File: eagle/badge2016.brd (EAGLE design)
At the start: 124.2 x 92.5 mm, 82 parts, among them IC1 FT230XS, IC3 24AA01SN, J1 USB-MICRO, Q2 BC857ALT1SMD, X1 PASSER-07, X2 PASSER-07, X3 PASSER-07

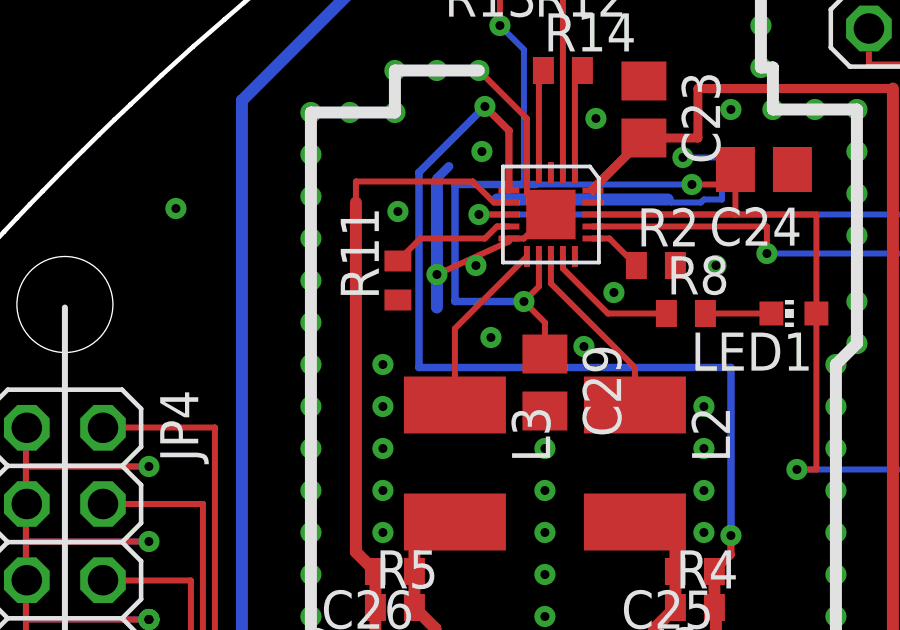
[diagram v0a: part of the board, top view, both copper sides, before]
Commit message: Update Layout changes by LTC3554 review
Review and changes LTC3554:
* Missing connecting Pin 9 (PWR_ON1) via R11 to Pin 18 (V_OUT) to activate SW1
* Change R2 from 1.87k to 750 (for max. load of 1A)
* PIN 15 (NTC) to GND, because NTC is not in use
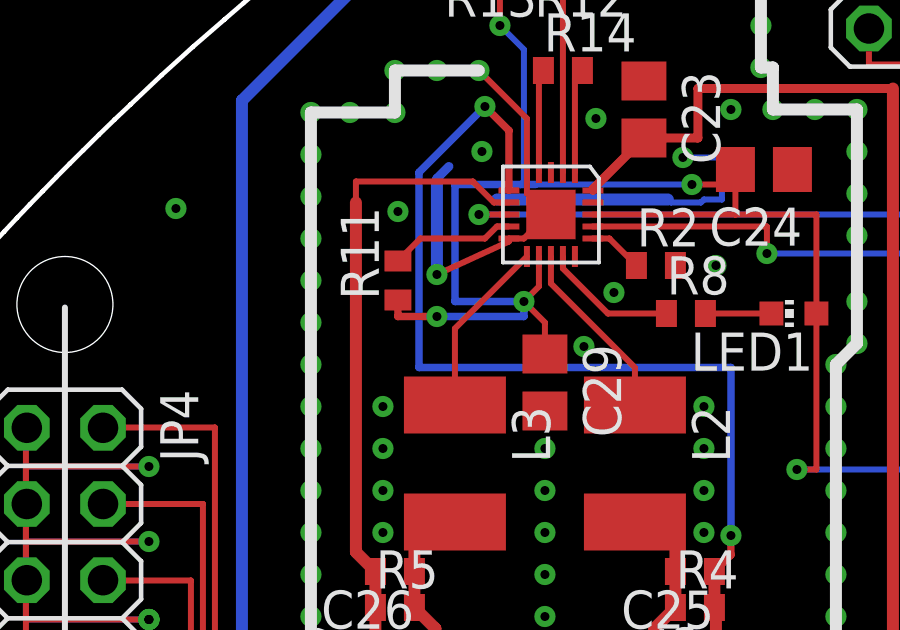
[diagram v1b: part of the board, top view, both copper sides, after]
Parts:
- R2: value 1.87k -> 750
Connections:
- removed net N$24: R11.1
- net GND: now also U$11.15
- net V_USB: now also R11.1
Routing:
- net V_USB: track 103.5 -> 108.7 mm, vias 7 -> 8
- net GND: track 298.7 -> 297.6 mm, vias 201 -> 198
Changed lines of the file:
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@@
 <element name="U$10" library="ERNW_parts" package="SMA_CON_THT" value="SMA_CONNECTORTHT" x="107.83" y="57.5"/>
 <element name="U$11" library="ERNW_parts" package="QFN-20-3X3" value="LTC3554" x="30.1" y="63" rot="R270"/>
-<element name="R2" library="rcl" package="R0402" value="1.87k" x="33.6" y="61.3"/>
+<element name="R2" library="rcl" package="R0402" value="750" x="33.6" y="61.3"/>
 <element name="C23" library="rcl" package="C0805" value="10µF" x="33.2" y="66.5" rot="R270"/>
 <element name="C24" library="rcl" package="C0805" value="10µF" x="37.2" y="64.5" rot="R180"/>
@@
 <wire x1="105.29" y1="60.04" x2="110.37" y2="60.04" width="0.4" layer="1"/>
 <wire x1="110.37" y1="60.04" x2="110.37" y2="54.96" width="0.4" layer="1"/>
-<contactref element="R2" pad="2"/>
 <contactref element="C23" pad="1"/>
 <contactref element="C24" pad="1"/>
@@
 <wire x1="54.4" y1="44.495" x2="54.4" y2="44.4" width="0.2" layer="1"/>
 <via x="68" y="47" extent="1-16" drill="0.3"/>
-<via x="27.6" y="61.3" extent="1-16" drill="0.3"/>
 <via x="26.3" y="61" extent="1-16" drill="0.3"/>
-<via x="28.1" y="58.9" extent="1-16" drill="0.3"/>
 <via x="32.2" y="60.4" extent="1-16" drill="0.3"/>
 <via x="27.8" y="65.1" extent="1-16" drill="0.3"/>
@@
 <via x="24.5" y="53.8" extent="1-16" drill="0.3"/>
 <via x="24.5" y="52.4" extent="1-16" drill="0.3"/>
-<via x="24.5" y="58" extent="1-16" drill="0.3"/>
 <via x="78.2" y="53.6" extent="1-16" drill="0.3"/>
 <via x="39.6" y="42.6" extent="1-16" drill="0.3"/>
@@
 <via x="51.6" y="76.6" extent="1-16" drill="0.3"/>
 <wire x1="26.3" y1="61" x2="26.3" y2="64.1" width="0.4" layer="16"/>
-<wire x1="26.3" y1="61" x2="26.3" y2="59.9" width="0.4" layer="16"/>
 <wire x1="26.3" y1="64.1" x2="26.3" y2="64.2" width="0.3" layer="16"/>
 <wire x1="26.3" y1="64.2" x2="26.7" y2="64.6" width="0.3" layer="16"/>
@@
 <wire x1="34.1" y1="63.4" x2="34" y2="63.5" width="0.2" layer="16"/>
 <wire x1="34" y1="63.5" x2="28.3" y2="63.5" width="0.4" layer="16"/>
+<contactref element="U$11" pad="15"/>
+<contactref element="R2" pad="2"/>
+<wire x1="30.1" y1="63" x2="30.9" y2="61.6" width="0" layer="19" extent="1-1"/>
 </signal>
 <signal name="3V3">
@@
 <wire x1="32.9" y1="57.9" x2="32.9" y2="56.65" width="0.2" layer="1"/>
 </signal>
-<signal name="N$24">
-<contactref element="R11" pad="1"/>
-</signal>
 <signal name="FB1">
 <contactref element="U$11" pad="6"/>
@@
 <wire x1="29.2" y1="68.5" x2="29.2" y2="64.1" width="0.2" layer="16"/>
 <wire x1="29.2" y1="64.1" x2="29.1" y2="64" width="0.2" layer="16"/>
+<contactref element="R11" pad="1"/>
+<wire x1="25" y1="60.15" x2="25" y2="59.6" width="0.25" layer="1"/>
+<wire x1="25" y1="59.6" x2="26.3" y2="59.6" width="0.25" layer="1"/>
+<wire x1="25" y1="60.15" x2="25" y2="60.15" width="0" layer="19" extent="1-16"/>
+<via x="26.3" y="59.6" extent="1-16" drill="0.3"/>
+<wire x1="26.3" y1="59.6" x2="29.2" y2="59.6" width="0.25" layer="16"/>
+<wire x1="29.2" y1="59.6" x2="29.2" y2="60.1" width="0.25" layer="16"/>
 </signal>
 <signal name="CTS#">
@@
 <wire x1="38" y1="22.9" x2="43.45" y2="22.9" width="0.15" layer="1"/>
 <wire x1="43.45" y1="22.9" x2="43.45" y2="22.5" width="0.15" layer="1"/>
+<wire x1="35.5925" y1="19.04848125" x2="35.592496875" y2="19.04848125" width="0" layer="19" extent="1-1"/>
 </signal>
 <signal name="DM">

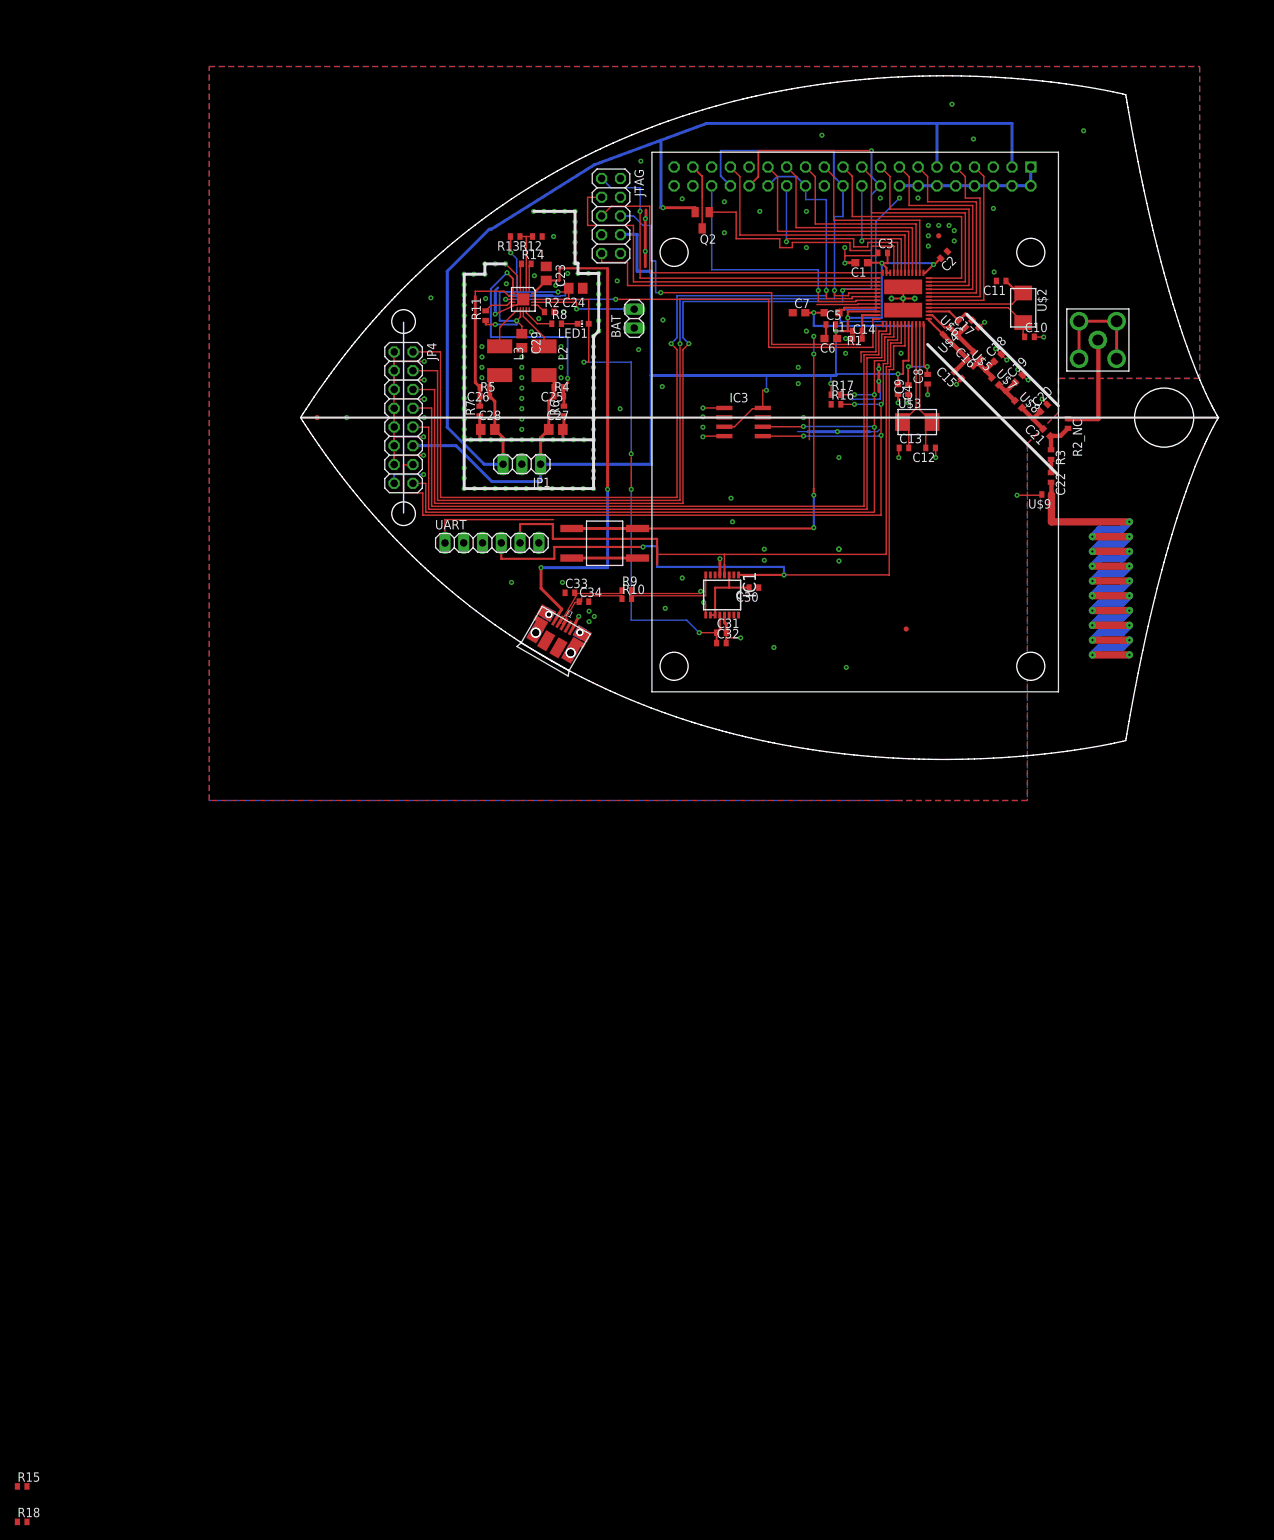
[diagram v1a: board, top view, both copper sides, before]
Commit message: New Display New USB <-> Serial + Connection to Power Supply Chip Moved Power Supply Chip, UART und JTAG Headers Changed Expansion Header
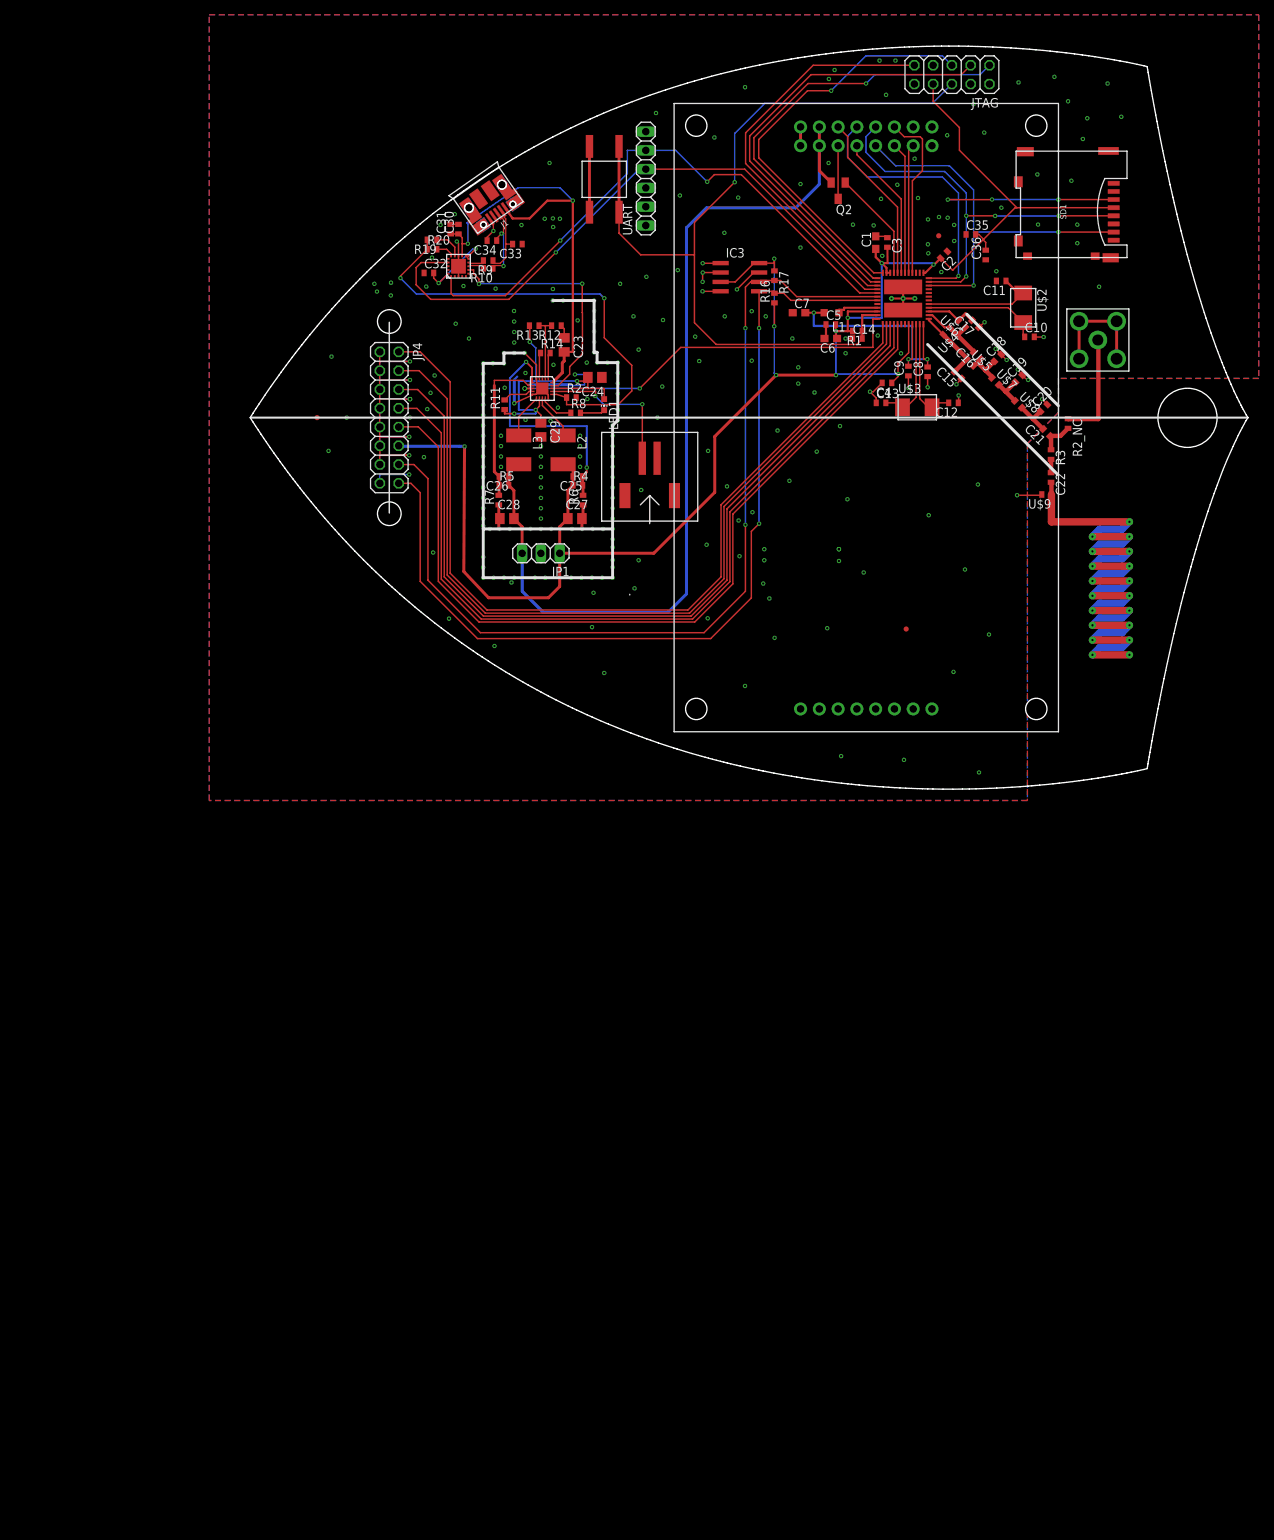
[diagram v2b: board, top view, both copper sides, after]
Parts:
- removed BAT: (no value), pinhead:1X02
- removed IC1: FT230XS, ftdichip:SSOP16
- removed R15, R18: 100k, rcl:R0402
- added C35: 100nF, rcl:C0402
- added C36: 4.7µF, rcl:C0402
- added R19: 4k32, rcl:R0402
- added R20: 1k5, rcl:R0402
- added SD1: SD-CARD-MSD50, we-con:SD_5031821853
- added U$14: MI0283QT, ERNW_parts:MI0283QT
- added U$15: JST-2, ERNW_parts:JST-2
- C31: value 100nF -> 4.7µF
- C32: value 4.7µF -> 100nF
- R2: value 750 -> 16k5
- U$12: value SAINSMART_2.4_TFT -> FT231X; device ERNW_parts:SAINSMART_2.4_TFT -> ERNW_parts:QFN-20-4X4
- moved C31 65.7 mm to (20.3, 72.5), turned to 90 degrees
- moved C32 63.8 mm to (17.3, 66.6)
- moved C30 62.9 mm to (21.3, 72.5), turned to 90 degrees
- moved J1 61.1 mm to (25.0, 76.9), turned to 125 degrees
- moved UART 53.5 mm to (46.7, 79.3), turned to 90 degrees
- moved C34 50.4 mm to (25.9, 71.0), turned to 180 degrees
- moved JTAG 49.9 mm to (88.1, 93.4), turned to 180 degrees
- moved U$13 49.2 mm to (41.0, 79.2), turned to 270 degrees
- moved R10 48.5 mm to (25.4, 67.2), turned to 180 degrees
- moved R9 48.4 mm to (25.4, 68.2), turned to 180 degrees
- moved C33 47.7 mm to (29.3, 70.5), turned to 180 degrees
- moved U$12 32.1 mm to (21.3, 67.5), turned to 90 degrees
- moved IC3 19.6 mm to (59.4, 66.0)
- moved Q2 18.8 mm to (72.7, 77.7)
- moved R17 18.1 mm to (64.1, 66.2), turned to 270 degrees
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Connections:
- removed net CS: U$1.17, U$12.CS
- removed net DB10: U$1.10, U$12.DB10
- removed net DB11: U$1.11, U$12.DB11
- removed net DB12: U$1.12, U$12.DB12
- removed net DB13: U$1.14, U$12.DB13
- removed net DB14: U$1.15, U$12.DB14
- removed net DB15: U$1.16, U$12.DB15
- removed net DB8: U$1.8, U$12.DB8
- removed net DB9: U$1.9, U$12.DB9
- removed net N$16: R2.1, U$11.16
- removed net N$19: C30.2, IC1.10, IC1.11, IC1.3
- removed net N$21: R18.2, U$1.32
- removed net N$31: R15.1, U$1.37
- removed net REST: U$1.18, U$12.REST
- removed net RS: U$1.6, U$12.RS
- removed net SD_CS: U$1.31, U$12.SD_CS
- removed net T_CS: U$1.19, U$12.T_CS
- removed net T_IRQ: U$1.20, U$12.T_IRQ
- removed net WR: U$1.7, U$12.WR
- new net !BCD: R20.2, U$12.15
- new net !PWREN: R19.1, U$12.14
- new net !SLEEP: U$11.19, U$12.7
- new net D_!CS: U$1.19, U$14.!CS
- new net D_!RST: U$1.20, U$14.!RST
- new net D_ADS_!CS: U$1.18, U$14.!ADS-CS
- new net D_AUX: U$14.AUX
- new net D_BUSY: U$1.16, U$14.BUSY
- new net D_IRQ: U$1.17, U$14.IRQ
- new net IO3: JP4.6, U$1.39
- new net IO4: JP4.8, U$1.40
- new net IO5: JP4.10, U$1.41
- new net N$24: U$14.VREF
- new net N$26: U$14.VBAT
- new net N$34: U$1.14
- new net N$35: U$1.15
- new net N$37: C32.2, U$12.10, U$12.11, U$12.20
- new net N$46: SD1.DAT1
- new net N$47: SD1.DAT2
- new net PROG: R19.2, R2.1, R20.1, U$11.16
- new net SD_!CS: SD1.CS
- new net SD_SWITCH: SD1.SW2
- net 3V3: now also C35.2, C36.2, SD1.VCC
- net DM: now also U$12.9; no longer IC1.9
- net DP: now also U$12.8; no longer IC1.8
- net GND: now also C30.2, C32.1, C35.1, C36.1, SD1.GND, SD1.SW1, U$12.13, U$12.3, U$12.PAD, U$14.GND0, U$14.GND1, U$15.1; no longer BAT.1, C30.1, C32.2, IC1.13, IC1.5, U$12.DB0, U$12.DB1, U$12.DB2, U$12.DB3, U$12.DB4, U$12.DB5, U$12.DB6, U$12.DB7, U$12.GND
- net I2C_SCL: now also JP4.14, U$1.30; no longer JP4.16, U$1.40
- net I2C_SDA: now also JP4.16, U$1.31; no longer JP4.14, U$1.41
- net IO1: now also JP4.2, U$1.37; no longer JP4.8, U$1.38
- net IO2: now also JP4.4, U$1.38; no longer JP4.10, U$1.39
- net LED_A: now also U$14.LED; no longer U$12.LED_A
- net N$20: now also U$15.2; no longer BAT.2
- net RXD: now also U$1.29, U$12.1; no longer IC1.4, U$1.42
- net SPI_CLK: now also SD1.SCK, U$1.11, U$14.SCK; no longer JP4.6, U$1.28, U$12.SD_CLK, U$12.T_CLK
- net SPI_MISO: now also SD1.MISO, U$1.10, U$14.MISO; no longer JP4.2, U$1.30, U$12.SD_DO, U$12.T_DO
- net SPI_MOSI: now also SD1.MOSI, U$1.12, U$14.MOSI; no longer JP4.4, U$1.29, U$12.SD_DIN, U$12.T_DIN
- net TXD: now also U$1.28, U$12.17; no longer IC1.1, U$1.43
- net VUSB_IN: now also C30.1, C31.1, U$12.12
- net V_DISP: now also U$14.VCC0, U$14.VCC1; no longer U$12.RD, U$12.VCC
- net V_USB: no longer C31.1, C32.1, IC1.12
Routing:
- net IO3: track 0.00 -> 115.6 mm
- net IO4: track 0.00 -> 114.3 mm
- net IO5: track 0.00 -> 113.3 mm
- net GND: track 297.6 -> 195.8 mm, vias 198 -> 271
- net SPI_CLK: track 152.3 -> 56.4 mm, vias 3 -> 4
- net SPI_MOSI: track 151.0 -> 60.9 mm, vias 2 -> 4
- net SPI_MISO: track 135.7 -> 53.7 mm
- net 3V3: track 189.2 -> 256.9 mm, vias 7 -> 10
- net V_USB: track 108.7 -> 42.9 mm, vias 8 -> 4
- net PROG: track 0.00 -> 62.0 mm, vias 0 -> 2
- net SD_CS: track 38.3 -> 0.00 mm, vias 1 -> 0
- net REST: track 37.2 -> 0.00 mm
- net DB12: track 34.8 -> 0.00 mm
- net DB11: track 33.7 -> 0.00 mm
- net !SLEEP: track 0.00 -> 32.8 mm, vias 0 -> 2
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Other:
- board size 124.2 x 92.5 mm -> 135 x 100.5 mm
